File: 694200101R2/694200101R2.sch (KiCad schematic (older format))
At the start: 264 parts, among them J1 USB_C_Receptacle_USB2.0, J2 Conn_01x06_Male, SW1 MX_SW, SW10 MX_SW, SW100 MX_SW, SW101 MX_SW, SW102 MX_SW, SW103 MX_SW, SW104 MX_SW, SW105 MX_SW, SW106 MX_SW, SW107 MX_SW, SW108 SW_SPST, SW109 SW_SPDT, SW11 MX_SW, SW12 MX_SW, SW13 MX_SW, SW14 MX_SW, SW15 MX_SW, SW16 MX_SW, SW17 MX_SW, SW18 MX_SW, SW19 MX_SW, SW2 MX_SW, SW20 MX_SW, SW21 MX_SW, SW22 MX_SW, SW23 MX_SW, SW24 MX_SW, SW25 MX_SW, SW26 MX_SW, SW27 MX_SW, SW28 MX_SW, SW29 MX_SW, SW3 MX_SW, SW30 MX_SW, SW31 MX_SW, SW32 MX_SW, SW33 MX_SW, SW34 MX_SW, SW35 MX_SW, SW36 MX_SW, SW37 MX_SW, SW38 MX_SW, SW39 MX_SW, SW4 MX_SW, SW40 MX_SW, SW41 MX_SW, SW42 MX_SW, SW43 MX_SW, SW44 MX_SW, SW45 MX_SW, SW46 MX_SW, SW47 MX_SW, SW48 MX_SW, SW49 MX_SW, SW5 MX_SW, SW50 MX_SW, SW51 MX_SW, SW52 MX_SW, SW53 MX_SW, SW54 MX_SW, SW55 MX_SW, SW56 MX_SW, SW57 MX_SW, SW58 MX_SW, SW59 MX_SW, SW6 MX_SW, SW60 MX_SW, SW61 MX_SW, SW62 MX_SW, SW63 MX_SW, SW64 MX_SW, SW65 MX_SW, SW66 MX_SW, SW67 MX_SW, SW68 MX_SW, SW69 MX_SW, SW7 MX_SW, SW70 MX_SW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

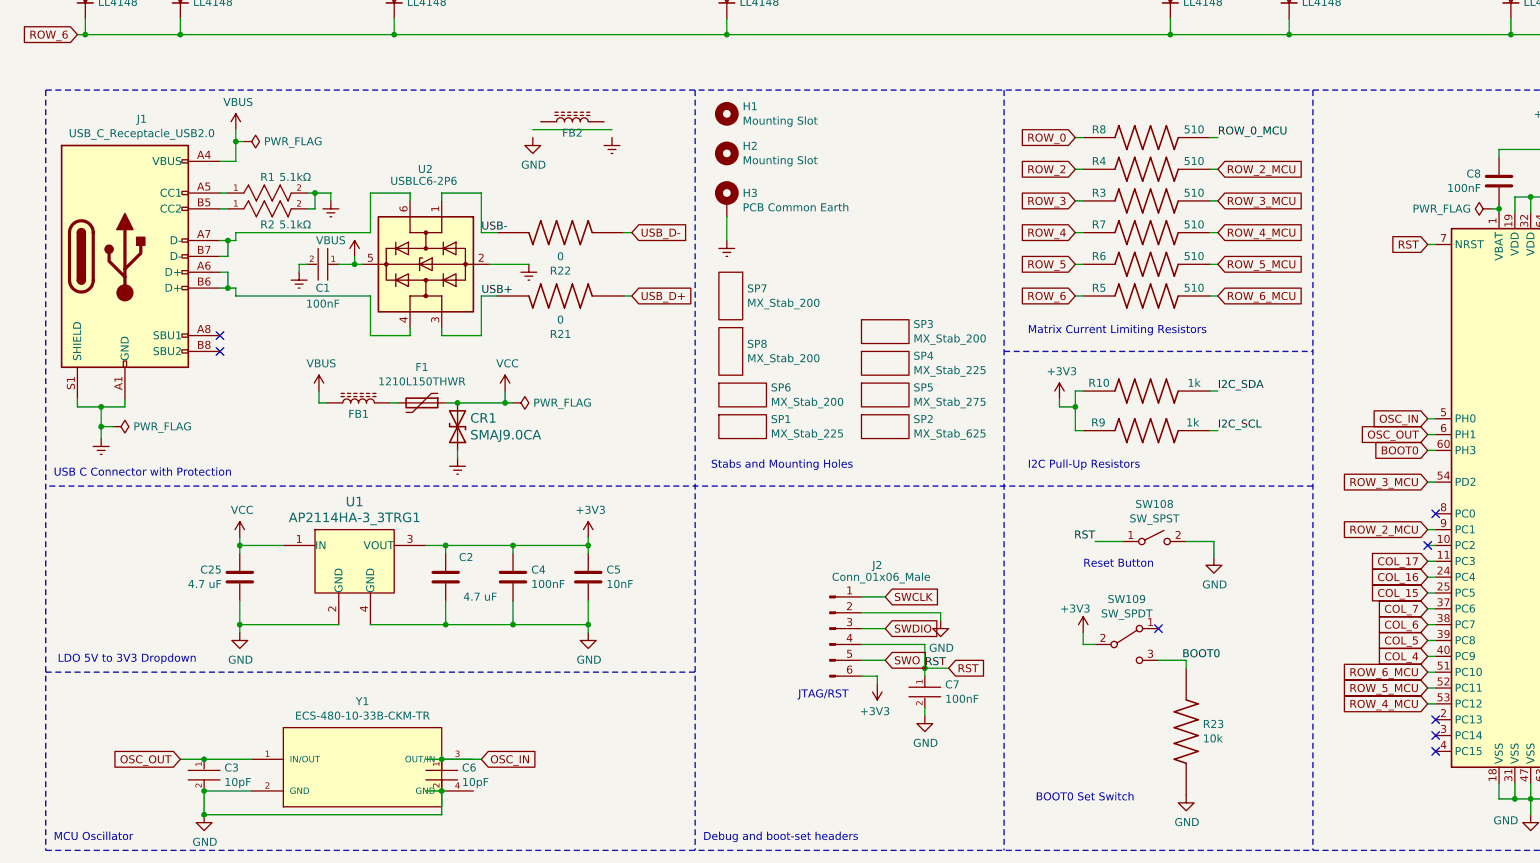
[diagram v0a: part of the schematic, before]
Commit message: Fixed merge issues in schematic
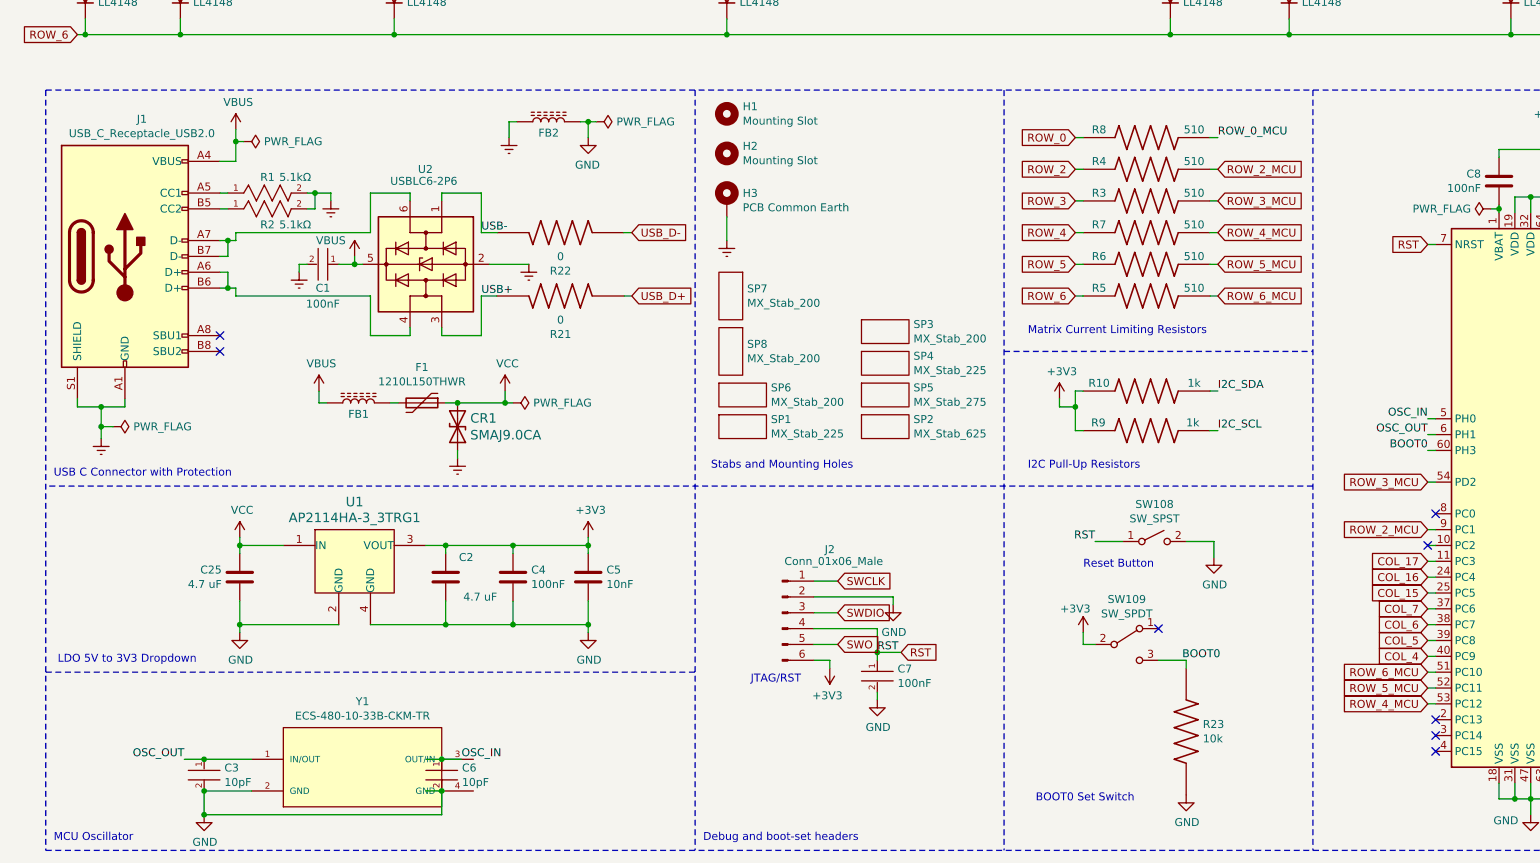
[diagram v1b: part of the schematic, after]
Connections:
- net Earth: now also FB2.1
- net GND: now also FB2.2
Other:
- moved on the sheet: C7, FB2, J2
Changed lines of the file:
@@
 L power:GND #PWR010
 U 1 1 6007927B
-P 6200 8850
-F 0 "#PWR010" H 6200 8600 50  0001 C CNN
-F 1 "GND" H 6205 8677 50  0000 C CNN
-F 2 "" H 6200 8850 50  0001 C CNN
-F 3 "" H 6200 8850 50  0001 C CNN
-	1    6200 8850
+P 5900 8750
+F 0 "#PWR010" H 5900 8500 50  0001 C CNN
+F 1 "GND" H 5905 8577 50  0000 C CNN
+F 2 "" H 5900 8750 50  0001 C CNN
+F 3 "" H 5900 8750 50  0001 C CNN
+	1    5900 8750
 	1    0    0    -1
 $EndComp
@@
 L capacitor-lib:CL10B104KB8NNNL C7
 U 1 1 600879ED
-P 6200 8600
-F 0 "C7" H 6328 8546 50  0000 L CNN
-F 1 "CL10B104KB8NNNL" H 6328 8455 50  0001 L CNN
-F 2 "Capacitor_SMD:C_0603_1608Metric" H 6200 8900 50  0001 L CNN
-F 3 "https://datasheet.octopart.com/CL02C050BO2GNNC-Samsung-Electro-Mechanics-datasheet-97040617.pdf" H 6200 9000 50  0001 L CNN
-F 4 "No" H 6200 9100 50  0001 L CNN "automotive"
-F 5 "100nF" H 6328 8455 50  0000 L CNN "capacitance"
-F 6 "Cap" H 6200 9300 50  0001 L CNN "category"
-F 7 "Passive Components" H 6200 9400 50  0001 L CNN "device class L1"
-F 8 "Capacitors" H 6200 9500 50  0001 L CNN "device class L2"
-F 9 "Ceramic Capacitors" H 6200 9600 50  0001 L CNN "device class L3"
-F 10 "" H 6200 9700 50  0001 L CNN "digikey description"
-F 11 "" H 6200 9800 50  0001 L CNN "digikey part number"
-F 12 "0.9mm" H 6200 9900 50  0001 L CNN "height"
-F 13 "CAPC16080X80" H 6200 10000 50  0001 L CNN "ipc land pattern name"
-F 14 "Yes" H 6200 10100 50  0001 L CNN "lead free"
-F 15 "d416e2ef1cbb0413" H 6200 10200 50  0001 L CNN "library id"
-F 16 "Samsung" H 6200 10300 50  0001 L CNN "manufacturer"
-F 17 "Ceramic" H 6200 10400 50  0001 L CNN "material"
-F 18 "0603" H 6200 10500 50  0001 L CNN "package"
-F 19 "Yes" H 6200 10600 50  0001 L CNN "rohs"
-F 20 "X7R" H 6200 10700 50  0001 L CNN "temperature characteristic"
-F 21 "0.15" H 6200 10800 50  0001 L CNN "temperature coefficient"
-F 22 "+125°C" H 6200 10900 50  0001 L CNN "temperature range high"
-F 23 "-55°C" H 6200 11000 50  0001 L CNN "temperature range low"
-F 24 "10%" H 6200 11100 50  0001 L CNN "tolerance"
-F 25 "50V" H 6200 11200 50  0001 L CNN "voltage rating"
-	1    6200 8600
+P 5900 8500
+F 0 "C7" H 6028 8446 50  0000 L CNN
+F 1 "CL10B104KB8NNNL" H 6028 8355 50  0001 L CNN
+F 2 "Capacitor_SMD:C_0603_1608Metric" H 5900 8800 50  0001 L CNN
+F 3 "https://datasheet.octopart.com/CL02C050BO2GNNC-Samsung-Electro-Mechanics-datasheet-97040617.pdf" H 5900 8900 50  0001 L CNN
+F 4 "No" H 5900 9000 50  0001 L CNN "automotive"
+F 5 "100nF" H 6028 8355 50  0000 L CNN "capacitance"
+F 6 "Cap" H 5900 9200 50  0001 L CNN "category"
+F 7 "Passive Components" H 5900 9300 50  0001 L CNN "device class L1"
+F 8 "Capacitors" H 5900 9400 50  0001 L CNN "device class L2"
+F 9 "Ceramic Capacitors" H 5900 9500 50  0001 L CNN "device class L3"
+F 10 "" H 5900 9600 50  0001 L CNN "digikey description"
+F 11 "" H 5900 9700 50  0001 L CNN "digikey part number"
+F 12 "0.9mm" H 5900 9800 50  0001 L CNN "height"
+F 13 "CAPC16080X80" H 5900 9900 50  0001 L CNN "ipc land pattern name"
+F 14 "Yes" H 5900 10000 50  0001 L CNN "lead free"
+F 15 "d416e2ef1cbb0413" H 5900 10100 50  0001 L CNN "library id"
+F 16 "Samsung" H 5900 10200 50  0001 L CNN "manufacturer"
+F 17 "Ceramic" H 5900 10300 50  0001 L CNN "material"
+F 18 "0603" H 5900 10400 50  0001 L CNN "package"
+F 19 "Yes" H 5900 10500 50  0001 L CNN "rohs"
+F 20 "X7R" H 5900 10600 50  0001 L CNN "temperature characteristic"
+F 21 "0.15" H 5900 10700 50  0001 L CNN "temperature coefficient"
+F 22 "+125°C" H 5900 10800 50  0001 L CNN "temperature range high"
+F 23 "-55°C" H 5900 10900 50  0001 L CNN "temperature range low"
+F 24 "10%" H 5900 11000 50  0001 L CNN "tolerance"
+F 25 "50V" H 5900 11100 50  0001 L CNN "voltage rating"
+	1    5900 8500
 	1    0    0    -1
 $EndComp
@@
 Connection ~ 7050 3250
 Wire Wire Line
-	5800 8100 5950 8100
-Text GLabel 5950 8100 2    50   Input ~ 0
+	5500 8000 5650 8000
+Text GLabel 5650 8000 2    50   Input ~ 0
 SWCLK
 Wire Wire Line
-	5800 8200 6300 8200
+	5500 8100 6000 8100
 $Comp
 L power:GND #PWR011
 U 1 1 602A2E5A
-P 6300 8250
-F 0 "#PWR011" H 6300 8000 50  0001 C CNN
-F 1 "GND" H 6305 8077 50  0000 C CNN
-F 2 "" H 6300 8250 50  0001 C CNN
-F 3 "" H 6300 8250 50  0001 C CNN
-	1    6300 8250
+P 6000 8150
+F 0 "#PWR011" H 6000 7900 50  0001 C CNN
+F 1 "GND" H 6005 7977 50  0000 C CNN
+F 2 "" H 6000 8150 50  0001 C CNN
+F 3 "" H 6000 8150 50  0001 C CNN
+	1    6000 8150
 	1    0    0    -1
 $EndComp
 Wire Wire Line
-	5800 8300 5950 8300
-Text GLabel 5950 8300 2    50   Input ~ 0
+	5500 8200 5650 8200
+Text GLabel 5650 8200 2    50   Input ~ 0
 SWDIO
 Wire Wire Line
-	6200 8400 5800 8400
+	5900 8300 5500 8300
 Wire Wire Line
-	5800 8500 5950 8500
-Text GLabel 5950 8500 2    50   Input ~ 0
+	5500 8400 5650 8400
+Text GLabel 5650 8400 2    50   Input ~ 0
 SWO
 Wire Wire Line
-	6200 8800 6200 8850
+	5900 8700 5900 8750
 $Comp
 L cldg:MX_Stab_225 SP1
@@
 	1    0    0    -1
 $EndComp
-Text Label 6200 8550 0    50   ~ 0
+Text Label 5900 8450 0    50   ~ 0
 RST
 Wire Wire Line
@@
 L power:+3V3 #PWR05
 U 1 1 62499D89
-P 5900 8650
-F 0 "#PWR05" H 5900 8500 50  0001 C CNN
-F 1 "+3V3" H 5915 8823 50  0000 C CNN
-F 2 "" H 5900 8650 50  0001 C CNN
-F 3 "" H 5900 8650 50  0001 C CNN
-	1    5900 8650
+P 5600 8550
+F 0 "#PWR05" H 5600 8400 50  0001 C CNN
+F 1 "+3V3" H 5615 8723 50  0000 C CNN
+F 2 "" H 5600 8550 50  0001 C CNN
+F 3 "" H 5600 8550 50  0001 C CNN
+	1    5600 8550
 	-1   0    0    1
 $EndComp
 Wire Wire Line
-	5900 8600 5900 8650
+	5600 8500 5600 8550
 Wire Wire Line
-	5900 8600 5800 8600
+	5600 8500 5500 8500
 $Comp
 L Resistor-Lib:RNCP0603FTD10K0 R23
@@
 $EndComp
 Wire Wire Line
-	1500 9125 1650 9125
+	1525 9125 1650 9125
 Wire Wire Line
 	1650 9475 3150 9475
@@
 L Connector:Conn_01x06_Male J2
 U 1 1 621CEF5F
-P 5600 8300
-F 0 "J2" H 5900 8700 50  0000 C CNN
-F 1 "Conn_01x06_Male" H 5925 8625 50  0000 C CNN
-F 2 "Connector_PinHeader_2.54mm:PinHeader_1x06_P2.54mm_Vertical" H 5600 8300 50  0001 C CNN
-F 3 "~" H 5600 8300 50  0001 C CNN
-	1    5600 8300
+P 5300 8200
+F 0 "J2" H 5600 8600 50  0000 C CNN
+F 1 "Conn_01x06_Male" H 5625 8525 50  0000 C CNN
+F 2 "Connector_PinHeader_2.54mm:PinHeader_1x06_P2.54mm_Vertical" H 5300 8200 50  0001 C CNN
+F 3 "~" H 5300 8200 50  0001 C CNN
+	1    5300 8200
 	1    0    0    -1
 $EndComp
 Wire Wire Line
-	3150 9125 3400 9125
+	3150 9125 3275 9125
 $Comp
 L capacitor-lib:06035A100JAT2A C3
@@
 	-1   0    0    1
 $EndComp
-Text GLabel 1500 9125 0    50   Input ~ 0
-OSC_OUT
-Text GLabel 3400 9125 2    50   Input ~ 0
-OSC_IN
 Wire Notes Line
 	4750 4900 4750 9700
@@
 MCU Oscillator
 Wire Wire Line
-	6200 8400 6200 8550
+	5900 8300 5900 8450
 Wire Wire Line
-	6300 8200 6300 8250
+	6000 8100 6000 8150
 Wire Wire Line
-	6200 8550 6350 8550
-Connection ~ 6200 8550
+	5900 8450 6050 8450
+Connection ~ 5900 8450
 Wire Wire Line
-	6200 8550 6200 8600
-Text GLabel 6350 8550 2    50   Input ~ 0
+	5900 8450 5900 8500
+Text GLabel 6050 8450 2    50   Input ~ 0
 RST
-Text Notes 5400 8750 0    50   ~ 0
+Text Notes 5100 8650 0    50   ~ 0
 JTAG/RST
 $Comp
@@
 Text GLabel 9375 5875 0    50   Input ~ 0
 RST
-Text GLabel 9375 7175 0    50   Input ~ 0
-BOOT0
-Text GLabel 9375 6975 0    50   Input ~ 0
-OSC_IN
-Text GLabel 9375 7075 0    50   Input ~ 0
-OSC_OUT
 $Comp
 L Resistor-Lib:RMCF0805FT510R R5
@@
 L power:GND #PWR02
 U 1 1 62F09F65
-P 3725 5200
-F 0 "#PWR02" H 3725 4950 50  0001 C CNN
-F 1 "GND" H 3730 5027 50  0000 C CNN
-F 2 "" H 3725 5200 50  0001 C CNN
-F 3 "" H 3725 5200 50  0001 C CNN
-	1    3725 5200
-	1    0    0    -1
+P 4075 5200
+F 0 "#PWR02" H 4075 4950 50  0001 C CNN
+F 1 "GND" H 4080 5027 50  0000 C CNN
+F 2 "" H 4075 5200 50  0001 C CNN
+F 3 "" H 4075 5200 50  0001 C CNN
+	1    4075 5200
+	-1   0    0    -1
 $EndComp
 $Comp
 L power:Earth #PWR031
 U 1 1 62F79601
-P 4225 5200
-F 0 "#PWR031" H 4225 4950 50  0001 C CNN
-F 1 "Earth" H 4225 5050 50  0001 C CNN
-F 2 "" H 4225 5200 50  0001 C CNN
-F 3 "~" H 4225 5200 50  0001 C CNN
-	1    4225 5200
-	1    0    0    -1
+P 3575 5200
+F 0 "#PWR031" H 3575 4950 50  0001 C CNN
+F 1 "Earth" H 3575 5050 50  0001 C CNN
+F 2 "" H 3575 5200 50  0001 C CNN
+F 3 "~" H 3575 5200 50  0001 C CNN
+	1    3575 5200
+	-1   0    0    -1
 $EndComp
 Text GLabel 12400 6125 0    50   Input ~ 0
@@
 L cldg:BBUP00160808600Y00 FB2
 U 1 1 633C94A9
-P 3925 5200
-F 0 "FB2" H 3875 5200 50  0000 C BNN
-F 1 "FBMJ3216HM600-T" H 3875 5434 50  0001 C CNN
-F 2 "Inductor_SMD:L_1206_3216Metric" H 3925 5200 50  0001 C CNN
-F 3 "" H 3925 5200 50  0001 C CNN
-	1    3925 5200
-	-1   0    0    -1
+P 3875 5200
+F 0 "FB2" H 3825 5200 50  0000 C BNN
+F 1 "FBMJ3216HM600-T" H 3825 5434 50  0001 C CNN
+F 2 "Inductor_SMD:L_1206_3216Metric" H 3875 5200 50  0001 C CNN
+F 3 "" H 3875 5200 50  0001 C CNN
+	1    3875 5200
+	1    0    0    -1
 $EndComp
 Wire Wire Line
@@
 $EndComp
 Wire Wire Line
-	3725 5150 4225 5150
+	3625 5100 3575 5100
+Wire Wire Line
+	3575 5100 3575 5200
+Wire Wire Line
+	4025 5100 4075 5100
+Wire Wire Line
+	4075 5100 4075 5200
+Text Label 9375 7175 2    50   ~ 0
+BOOT0
+$Comp
+L power:PWR_FLAG #FLG0104
+U 1 1 62CE59E5
+P 4125 5100
+F 0 "#FLG0104" H 4125 5175 50  0001 C CNN
+F 1 "PWR_FLAG" V 4125 5228 50  0000 L CNN
+F 2 "" H 4125 5100 50  0001 C CNN
+F 3 "~" H 4125 5100 50  0001 C CNN
+	1    4125 5100
+	0    1    -1   0
+$EndComp
+Wire Wire Line
+	4125 5100 4075 5100
+Connection ~ 4075 5100
+Text Label 9375 7075 2    50   ~ 0
+OSC_OUT
+Text Label 1525 9125 2    50   ~ 0
+OSC_OUT
+Text Label 9375 6975 2    50   ~ 0
+OSC_IN
+Text Label 3275 9125 0    50   ~ 0
+OSC_IN
 $EndSCHEMATC

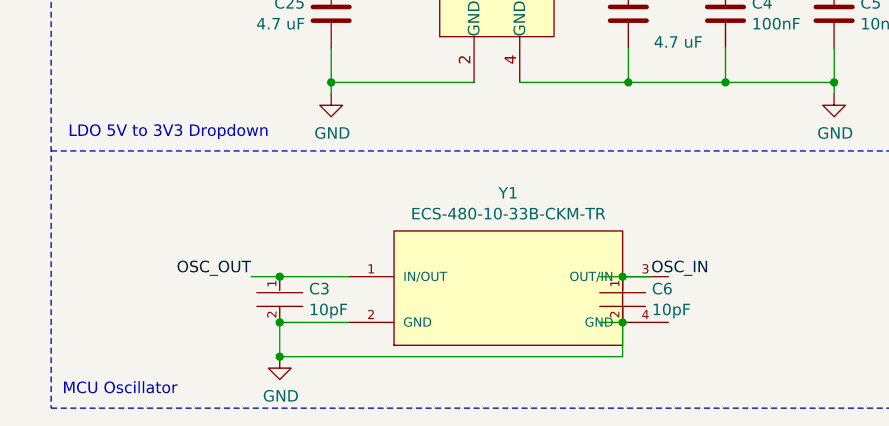
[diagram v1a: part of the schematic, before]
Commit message: Updated Crystal symbol
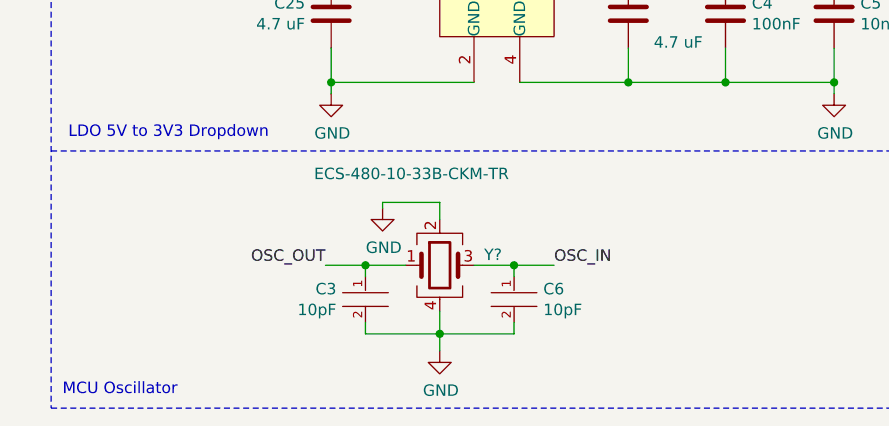
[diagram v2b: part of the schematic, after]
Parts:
- removed Y1: ECS-480-10-33B-CKM-TR, cldg:XTAL_ECS-480-10-33B-CKM-TR, symbol cldg:ECS-480-10-33B-CKM-TR
- added Y?: ECS-480-10-33B-CKM-TR, cldg:XTAL_ECS-480-10-33B-CKM-TR, symbol Device:Crystal_GND24
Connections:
- net GND: now also Y?.2, Y?.4
- net OSC_IN: now also Y?.3
- net OSC_OUT: now also Y?.1
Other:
- moved on the sheet: C3, C6

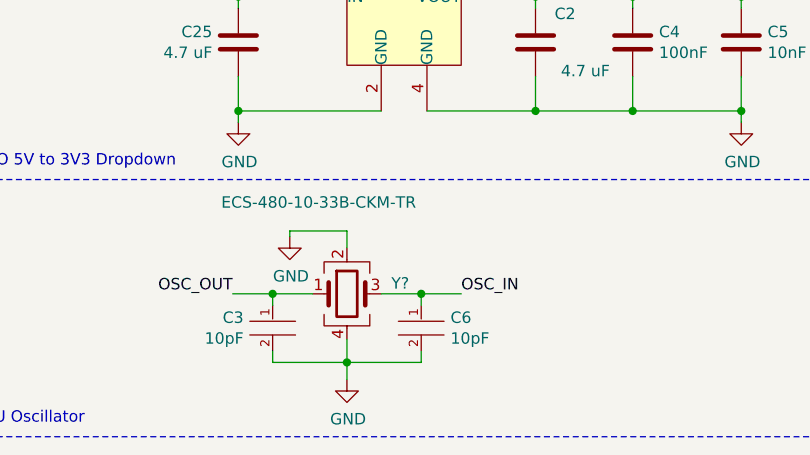
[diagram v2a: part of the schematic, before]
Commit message: Forgot Crystal Annotation
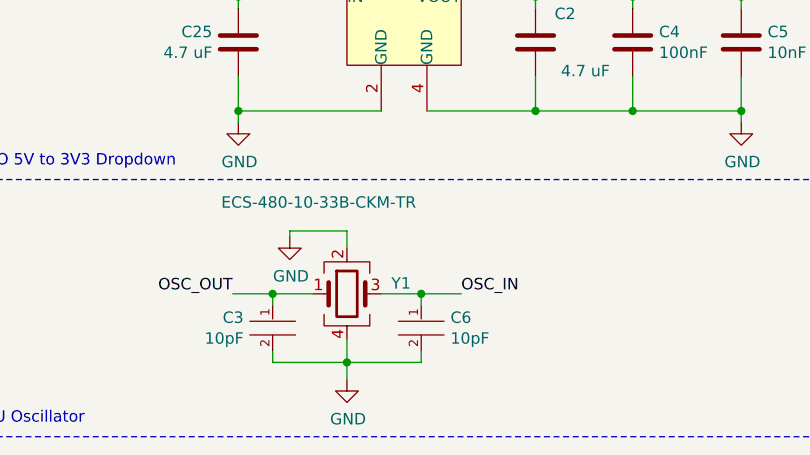
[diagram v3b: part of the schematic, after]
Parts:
- gave numbers to parts that had none: 1
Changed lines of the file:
@@
 $EndComp
 $Comp
-L Device:Crystal_GND24 Y?
+L Device:Crystal_GND24 Y1
 U 1 1 62F4C172
 P 2350 9075
-F 0 "Y?" H 2544 9121 50  0000 L CNN
+F 0 "Y1" H 2544 9121 50  0000 L CNN
 F 1 "ECS-480-10-33B-CKM-TR" H 1800 9475 50  0000 L CNN
 F 2 "cldg:XTAL_ECS-480-10-33B-CKM-TR" H 2350 9075 50  0001 C CNN
